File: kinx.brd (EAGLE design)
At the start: 122 x 86 mm, 45 parts, among them T1 MCP1825S

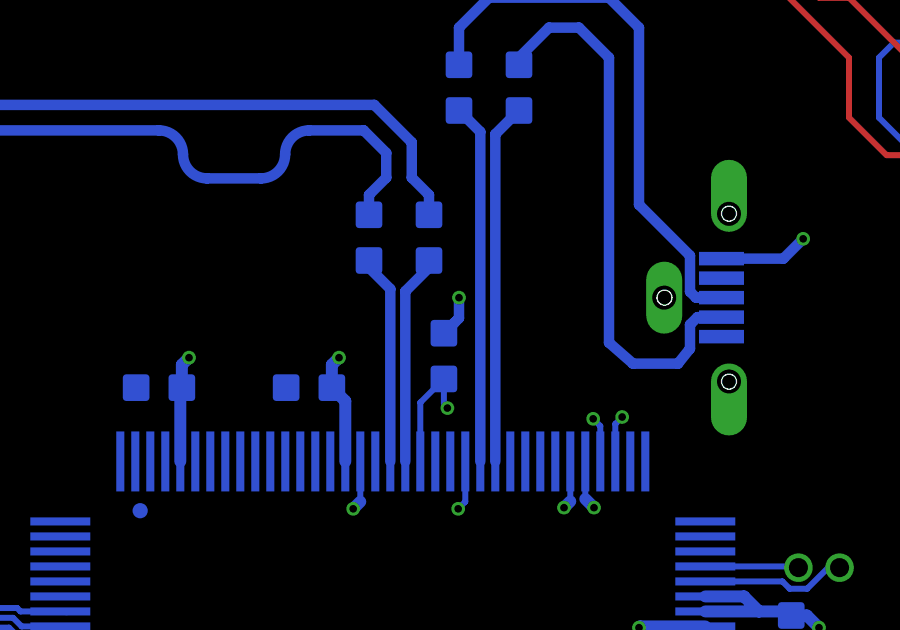
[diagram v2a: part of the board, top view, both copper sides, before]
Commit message: move via for clearance
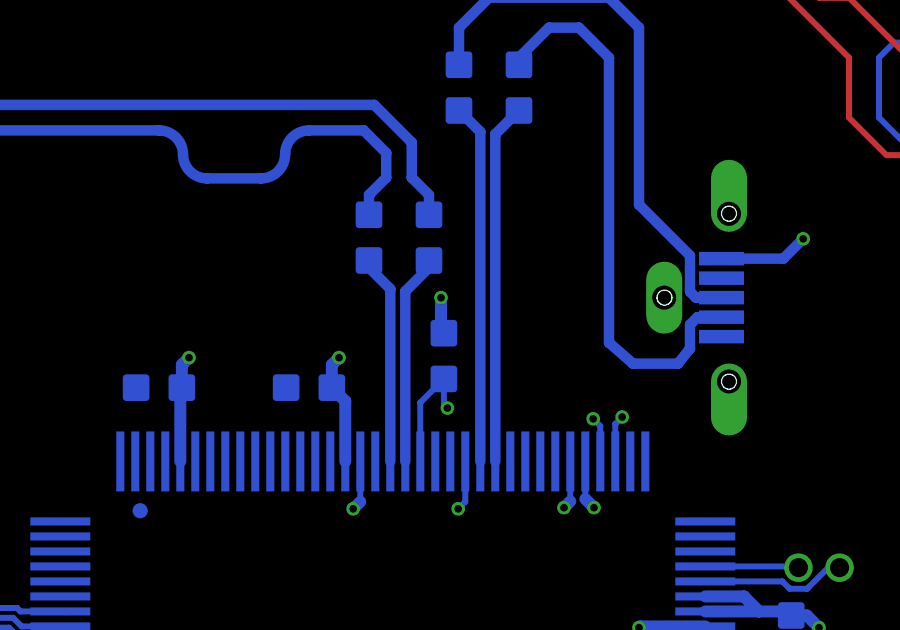
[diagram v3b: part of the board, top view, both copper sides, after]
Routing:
- net GND: track 27.4 -> 26.8 mm
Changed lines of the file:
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@@
 <wire x1="76.46" y1="52.54" x2="77" y2="52" width="0.2" layer="16"/>
 <via x="77" y="52" extent="1-16" drill="0.254"/>
-<wire x1="87.86" y1="64.177" x2="87.497" y2="63.814" width="0.35" layer="16"/>
-<via x="88" y="65" extent="1-16" drill="0.254"/>
+<via x="87.4" y="65" extent="1-16" drill="0.254"/>
 <contactref element="USBHS" pad="P$3"/>
 <contactref element="USBFS" pad="P$3"/>
 <contactref element="USBFS" pad="5"/>
 <contactref element="USBHS" pad="5"/>
-<wire x1="87.497" y1="63.814" x2="88" y2="64.317" width="0.35" layer="16"/>
-<wire x1="88" y1="64.317" x2="88" y2="65" width="0.35" layer="16"/>
 <via x="99.472" y="66.96" extent="1-16" drill="0.254"/>
 <wire x1="98.812" y1="66.3" x2="96.75" y2="66.3" width="0.35" layer="16"/>
@@
 <wire x1="88.21" y1="59.54" x2="88.21" y2="58.198" width="0.2" layer="16"/>
 <wire x1="88.21" y1="58.198" x2="87.972" y2="57.96" width="0.2" layer="16"/>
-<wire x1="120" y1="73" x2="120" y2="84" width="0" layer="19" extent="1-1"/>
-<wire x1="108" y1="84" x2="120" y2="84" width="0" layer="19" extent="1-1"/>
-<wire x1="120" y1="61" x2="120" y2="73" width="0" layer="19" extent="1-1"/>
-<wire x1="113.2606" y1="60.2512" x2="120" y2="61" width="0" layer="19" extent="1-1"/>
-<wire x1="113.2606" y1="53.7488" x2="113.2606" y2="60.2512" width="0" layer="19" extent="1-1"/>
-<wire x1="120" y1="49" x2="113.2606" y2="53.7488" width="0" layer="19" extent="1-1"/>
-<wire x1="120" y1="38" x2="120" y2="49" width="0" layer="19" extent="1-1"/>
-<wire x1="109.25" y1="40.523" x2="120" y2="38" width="0" layer="19" extent="16-16"/>
-<wire x1="109.6" y1="42.5074" x2="109.25" y2="40.523" width="0" layer="19" extent="16-16"/>
-<wire x1="108.8" y1="42.5074" x2="109.6" y2="42.5074" width="0" layer="19" extent="16-16"/>
-<wire x1="99" y1="42.762" x2="108.8" y2="42.5074" width="0" layer="19" extent="16-16"/>
-<wire x1="99" y1="46.238" x2="99" y2="42.762" width="0" layer="19" extent="16-16"/>
-<wire x1="96.21" y1="47.54" x2="99" y2="46.238" width="0" layer="19" extent="16-16"/>
-<wire x1="96.21" y1="40.54" x2="99" y2="42.762" width="0" layer="19" extent="16-16"/>
-<wire x1="96.098" y1="38.052" x2="96.21" y2="40.54" width="0" layer="19" extent="16-16"/>
-<wire x1="97.85" y1="36" x2="96.15" y2="38" width="0" layer="19" extent="16-16"/>
-<wire x1="99.075" y1="52.881" x2="96.21" y2="47.54" width="0" layer="19" extent="16-16"/>
-<wire x1="96.96" y1="54.04" x2="99.075" y2="52.881" width="0" layer="19" extent="16-16"/>
-<wire x1="93.21" y1="59.54" x2="94.04" y2="54.04" width="0" layer="19" extent="16-16"/>
-<wire x1="92.71" y1="59.54" x2="93.21" y2="59.54" width="0" layer="19" extent="16-16"/>
-<wire x1="97" y1="62.206" x2="93.439" y2="61.021" width="0" layer="19" extent="1-1"/>
-<wire x1="94.841" y1="65" x2="97" y2="62.206" width="0" layer="19" extent="1-1"/>
-<wire x1="96.75" y1="66.3" x2="94.841" y2="65" width="0" layer="19" extent="16-16"/>
-<wire x1="97" y1="67.794" x2="96.75" y2="66.3" width="0" layer="19" extent="16-16"/>
-<wire x1="88.21" y1="59.54" x2="92.472" y2="60.96" width="0" layer="19" extent="16-16"/>
-<wire x1="85.21" y1="59.54" x2="88.21" y2="59.54" width="0" layer="19" extent="16-16"/>
+<wire x1="87.4" y1="65" x2="87.4" y2="63.911" width="0.4" layer="16"/>
+<wire x1="87.4" y1="63.911" x2="87.497" y2="63.814" width="0.4" layer="16"/>
 <wire x1="84.71" y1="59.54" x2="85.21" y2="59.54" width="0" layer="19" extent="16-16"/>
-<wire x1="82.238" y1="62" x2="84.71" y2="59.54" width="0" layer="19" extent="16-16"/>
-<wire x1="79.21" y1="59.54" x2="82.238" y2="62" width="0" layer="19" extent="16-16"/>
-<wire x1="77.238" y1="62" x2="79.21" y2="59.54" width="0" layer="19" extent="16-16"/>
-<wire x1="87.497" y1="63.814" x2="88.21" y2="59.54" width="0" layer="19" extent="16-16"/>
-<wire x1="76.46" y1="52.54" x2="79.21" y2="59.54" width="0" layer="19" extent="16-16"/>
-<wire x1="70.238" y1="53" x2="74.71" y2="52.54" width="0" layer="19" extent="16-16"/>
-<wire x1="74.71" y1="46.04" x2="77" y2="52" width="0" layer="19" extent="16-16"/>
-<wire x1="77.494" y1="39.574" x2="74.71" y2="46.04" width="0" layer="19" extent="16-16"/>
-<wire x1="74.793" y1="36.525" x2="77.21" y2="38.04" width="0" layer="19" extent="16-16"/>
-<wire x1="82.194" y1="35.627" x2="77.21" y2="38.04" width="0" layer="19" extent="16-16"/>
-<wire x1="84.208" y1="36.827" x2="82.194" y2="35.627" width="0" layer="19" extent="16-16"/>
-<wire x1="67.238" y1="36" x2="74.793" y2="36.525" width="0" layer="19" extent="16-16"/>
-<wire x1="96" y1="84" x2="108" y2="84" width="0" layer="19" extent="1-1"/>
-<wire x1="84" y1="84" x2="96" y2="84" width="0" layer="19" extent="1-1"/>
-<wire x1="73" y1="84" x2="84" y2="84" width="0" layer="19" extent="1-1"/>
-<wire x1="61" y1="84" x2="73" y2="84" width="0" layer="19" extent="1-1"/>
-<wire x1="120" y1="26" x2="120" y2="38" width="0" layer="19" extent="1-1"/>
-<wire x1="49" y1="84" x2="61" y2="84" width="0" layer="19" extent="1-1"/>
-<wire x1="38" y1="84" x2="49" y2="84" width="0" layer="19" extent="1-1"/>
-<wire x1="40" y1="73.175" x2="38" y2="84" width="0" layer="19" extent="16-16"/>
-<wire x1="40" y1="66.825" x2="40" y2="73.175" width="0" layer="19" extent="16-16"/>
-<wire x1="47" y1="70.984" x2="40" y2="73.175" width="0" layer="19" extent="16-16"/>
-<wire x1="32" y1="71.238" x2="40" y2="73.175" width="0" layer="19" extent="16-16"/>
-<wire x1="28.016" y1="70" x2="32" y2="71.238" width="0" layer="19" extent="16-16"/>
-<wire x1="26.5" y1="63.694" x2="28.016" y2="70" width="0" layer="19" extent="16-16"/>
-<wire x1="26.25" y1="62.2" x2="26.5" y2="63.694" width="0" layer="19" extent="16-16"/>
-<wire x1="24.341" y1="60.9" x2="26.25" y2="62.2" width="0" layer="19" extent="16-16"/>
-<wire x1="26.5" y1="58.106" x2="24.341" y2="60.9" width="0" layer="19" extent="1-1"/>
-<wire x1="120" y1="14" x2="120" y2="26" width="0" layer="19" extent="1-1"/>
-<wire x1="120" y1="2" x2="120" y2="14" width="0" layer="19" extent="1-1"/>
-<wire x1="26" y1="84" x2="38" y2="84" width="0" layer="19" extent="1-1"/>
-<wire x1="14" y1="84" x2="26" y2="84" width="0" layer="19" extent="1-1"/>
-<wire x1="2" y1="84" x2="14" y2="84" width="0" layer="19" extent="1-1"/>
-<wire x1="2" y1="73" x2="2" y2="84" width="0" layer="19" extent="1-1"/>
-<wire x1="2" y1="61" x2="2" y2="73" width="0" layer="19" extent="1-1"/>
-<wire x1="2" y1="49" x2="2" y2="61" width="0" layer="19" extent="1-1"/>
-<wire x1="2" y1="38" x2="2" y2="49" width="0" layer="19" extent="1-1"/>
-<wire x1="2" y1="26" x2="2" y2="38" width="0" layer="19" extent="1-1"/>
-<wire x1="2" y1="14" x2="2" y2="26" width="0" layer="19" extent="1-1"/>
-<wire x1="2" y1="2" x2="2" y2="14" width="0" layer="19" extent="1-1"/>
-<wire x1="51.81" y1="39.81" x2="67.238" y2="36" width="0" layer="19" extent="16-16"/>
-<wire x1="51.81" y1="32.19" x2="51.81" y2="39.81" width="0" layer="19" extent="1-1"/>
-<wire x1="88.81" y1="13.73" x2="82.194" y2="35.627" width="0" layer="19" extent="16-16"/>
-<wire x1="88.81" y1="11.19" x2="88.81" y2="13.73" width="0" layer="19" extent="1-1"/>
 </signal>
 <signal name="N$12">

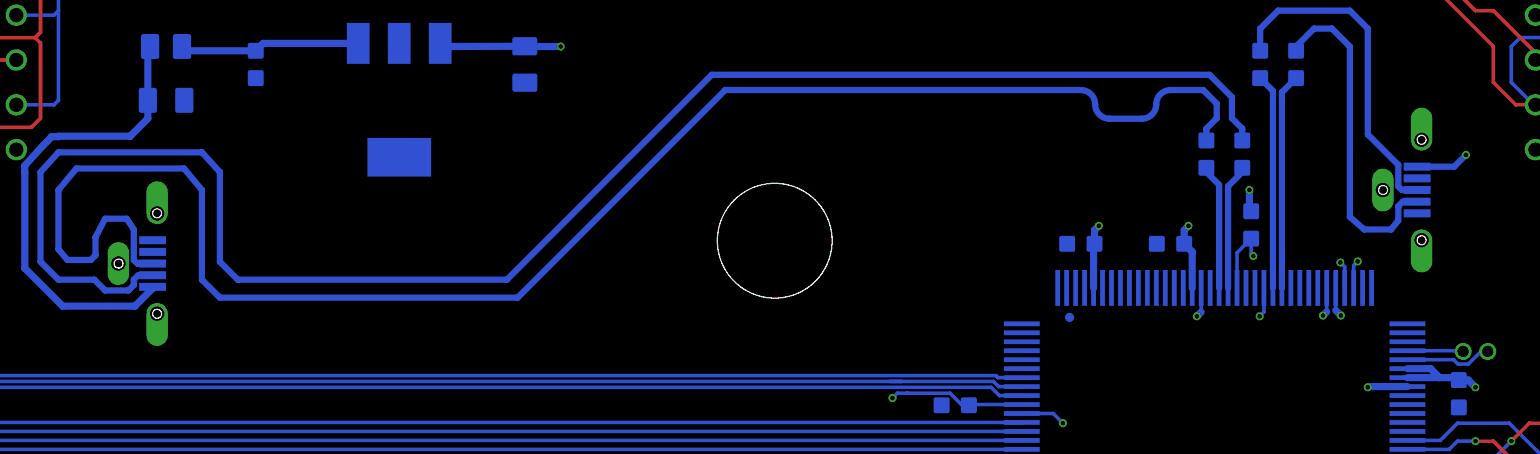
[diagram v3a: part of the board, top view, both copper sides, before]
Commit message: Fix Molex connector pads
As per the PCB layout from the drawing:
http://www.molex.com/pdm_docs/sd/1051330001_sd.pdf
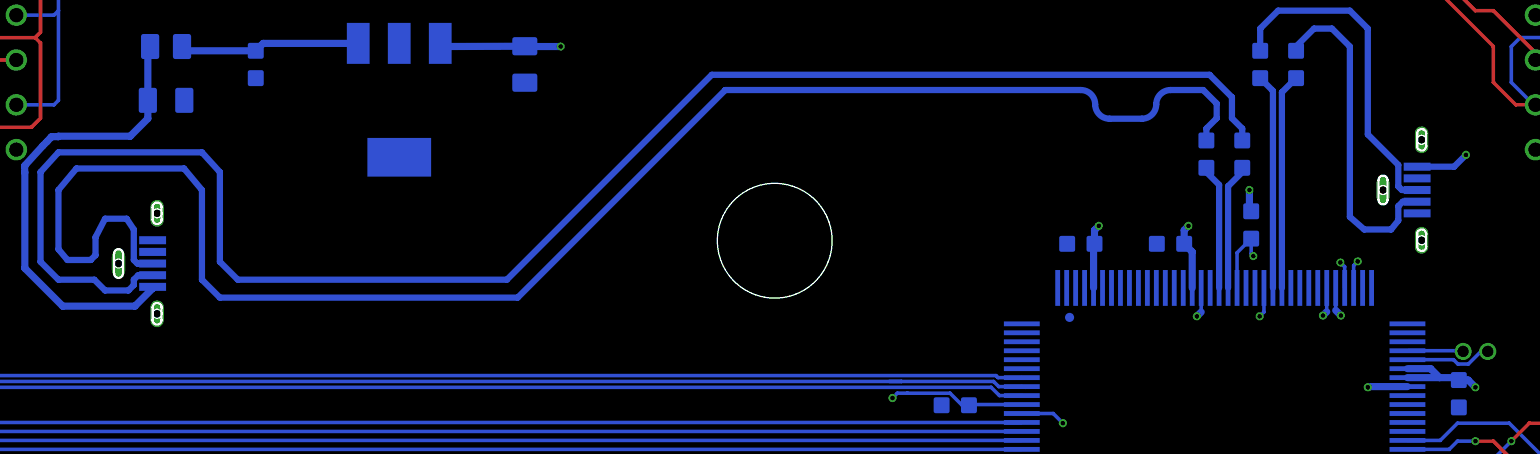
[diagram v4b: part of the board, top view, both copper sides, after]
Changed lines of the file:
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@@
 <layer number="44" name="Drills" color="7" fill="1" visible="no" active="yes"/>
 <layer number="45" name="Holes" color="7" fill="1" visible="yes" active="yes"/>
-<layer number="46" name="Milling" color="3" fill="1" visible="no" active="yes"/>
+<layer number="46" name="Milling" color="3" fill="1" visible="yes" active="yes"/>
 <layer number="47" name="Measures" color="7" fill="1" visible="no" active="yes"/>
 <layer number="48" name="Document" color="7" fill="1" visible="yes" active="yes"/>
@@
 <wire x1="87.4" y1="65" x2="87.4" y2="63.911" width="0.4" layer="16"/>
 <wire x1="87.4" y1="63.911" x2="87.497" y2="63.814" width="0.4" layer="16"/>
-<wire x1="84.71" y1="59.54" x2="85.21" y2="59.54" width="0" layer="19" extent="16-16"/>
+<wire x1="96.75" y1="66.3" x2="97" y2="67.8" width="0" layer="19" extent="16-16"/>
+<wire x1="85.21" y1="59.54" x2="84.71" y2="59.54" width="0" layer="19" extent="16-16"/>
+<wire x1="26.5" y1="63.7" x2="26.25" y2="62.2" width="0" layer="19" extent="16-16"/>
+<wire x1="94.85" y1="65" x2="96.75" y2="66.3" width="0" layer="19" extent="16-16"/>
+<wire x1="24.35" y1="60.9" x2="26.25" y2="62.2" width="0" layer="19" extent="16-16"/>
+<wire x1="97" y1="62.2" x2="94.85" y2="65" width="0" layer="19" extent="1-1"/>
+<wire x1="26.5" y1="58.1" x2="24.35" y2="60.9" width="0" layer="19" extent="1-1"/>
 </signal>
 <signal name="N$12">
